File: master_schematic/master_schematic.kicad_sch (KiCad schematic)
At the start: 8 parts, among them Q1 IRLZ34NPBF, U1 teensy_4.1

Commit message: PT update
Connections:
- net GND: now also U1.USB_GND1 (USB_GND), U1.USB_GND2 (USB_GND)
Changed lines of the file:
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@@
 	(paper "A4")
+	(junction
+		(at 181.61 152.4)
+		(diameter 0)
+		(color 0 0 0 0)
+	)
 	(junction
 		(at 234.95 22.86)
@@
 	(wire
 		(pts
+			(xy 173.99 152.4) (xy 181.61 152.4)
+		)
+		(stroke
+			(width 0)
+			(type default)
+		)
+	)
+	(wire
+		(pts
 			(xy 50.8 99.06) (xy 55.88 99.06)
 		)
@@
 		)
 	)
+	(wire
+		(pts
+			(xy 184.15 50.8) (xy 184.15 55.88)
+		)
+		(stroke
+			(width 0)
+			(type default)
+		)
+	)
 	(bus
 		(pts
@@
 		)
 	)
+	(wire
+		(pts
+			(xy 181.61 149.86) (xy 181.61 152.4)
+		)
+		(stroke
+			(width 0)
+			(type default)
+		)
+	)
 	(bus
 		(pts
@@
 	(wire
 		(pts
-			(xy 181.61 55.88) (xy 173.99 55.88)
+			(xy 184.15 55.88) (xy 173.99 55.88)
 		)
 		(stroke
@@
 		)
 	)
+	(wire
+		(pts
+			(xy 201.93 55.88) (xy 201.93 62.23)
+		)
+		(stroke
+			(width 0)
+			(type default)
+		)
+	)
 	(bus
 		(pts
@@
 		(pts
 			(xy 227.33 22.86) (xy 227.33 24.13)
-		)
-		(stroke
-			(width 0)
-			(type default)
-		)
-	)
-	(wire
-		(pts
-			(xy 181.61 50.8) (xy 181.61 55.88)
 		)
 		(stroke
@@
 		)
 	)
-	(label "5V"
+	(label "+5V"
 		(at 177.8 55.88 0)
 		(fields_autoplaced yes)
@@
 		)
 	)
-	(label "5V"
+	(label "+5V"
 		(at 156.21 21.59 180)
 		(fields_autoplaced yes)
@@
 	)
 	(label "GND"
-		(at 181.61 149.86 0)
+		(at 176.53 149.86 0)
 		(fields_autoplaced yes)
 		(effects
@@
 		)
 	)
-	(label "5V"
+	(label "+5V"
 		(at 45.72 158.75 270)
 		(fields_autoplaced yes)
@@
 		)
 	)
+	(global_label "GND"
+		(shape bidirectional)
+		(at 201.93 55.88 90)
+		(fields_autoplaced yes)
+		(effects
+			(font
+				(size 1.27 1.27)
+			)
+			(justify left)
+		)
+		(property "Intersheetrefs" "${INTERSHEET_REFS}"
+			(at 201.93 47.913 90)
+			(effects
+				(font
+					(size 1.27 1.27)
+				)
+				(justify left)
+				(hide yes)
+			)
+		)
+	)
+	(global_label "+5V"
+		(shape bidirectional)
+		(at 193.04 58.42 270)
+		(fields_autoplaced yes)
+		(effects
+			(font
+				(size 1.27 1.27)
+			)
+			(justify right)
+		)
+		(property "Intersheetrefs" "${INTERSHEET_REFS}"
+			(at 193.04 66.387 90)
+			(effects
+				(font
+					(size 1.27 1.27)
+				)
+				(justify right)
+				(hide yes)
+			)
+		)
+	)
 	(symbol
 		(lib_id "power:+5V")
-		(at 181.61 50.8 0)
+		(at 184.15 50.8 0)
 		(unit 1)
 		(exclude_from_sim no)
@@
 		(fields_autoplaced yes)
 		(property "Reference" "#PWR01"
-			(at 181.61 54.61 0)
+			(at 184.15 54.61 0)
 			(effects
 				(font
@@
 		)
 		(property "Value" "+5V"
-			(at 181.61 45.72 0)
+			(at 184.15 45.72 0)
 			(effects
 				(font
@@
 		)
 		(property "Footprint" ""
-			(at 181.61 50.8 0)
+			(at 184.15 50.8 0)
 			(effects
 				(font
@@
 		)
 		(property "Datasheet" ""
-			(at 181.61 50.8 0)
+			(at 184.15 50.8 0)
 			(effects
 				(font
@@
 		)
 		(property "Description" "Power symbol creates a global label with name \"+5V\""
-			(at 181.61 50.8 0)
+			(at 184.15 50.8 0)
 			(effects
 				(font
@@
 	)
 	(symbol
+		(lib_id "power:GND")
+		(at 201.93 62.23 0)
+		(unit 1)
+		(exclude_from_sim no)
+		(in_bom yes)
+		(on_board yes)
+		(dnp no)
+		(fields_autoplaced yes)
+		(property "Reference" "#PWR016"
+			(at 201.93 68.58 0)
+			(effects
+				(font
+					(size 1.27 1.27)
+				)
+				(hide yes)
+			)
+		)
+		(property "Value" "GND"
+			(at 201.93 67.31 0)
+			(effects
+				(font
+					(size 1.27 1.27)
+				)
+			)
+		)
+		(property "Footprint" ""
+			(at 201.93 62.23 0)
+			(effects
+				(font
+					(size 1.27 1.27)
+				)
+				(hide yes)
+			)
+		)
+		(property "Datasheet" ""
+			(at 201.93 62.23 0)
+			(effects
+				(font
+					(size 1.27 1.27)
+				)
+				(hide yes)
+			)
+		)
+		(property "Description" "Power symbol creates a global label with name \"GND\" , ground"
+			(at 201.93 62.23 0)
+			(effects
+				(font
+					(size 1.27 1.27)
+				)
+				(hide yes)
+			)
+		)
+		(pin "1"
+		)
+		(instances
+			(project ""
+				(path "/c4f7e98c-e88d-49cc-9841-b70710a90a72"
+					(reference "#PWR016")
+					(unit 1)
+				)
+			)
+		)
+	)
+	(symbol
 		(lib_id "hb_symbol_lib:radio_module_900MHz")
 		(at 171.45 17.78 0)
@@
 					(unit 1)
 				)
+			)
+		)
+	)
+	(symbol
+		(lib_id "power:GND")
+		(at 181.61 152.4 0)
+		(unit 1)
+		(exclude_from_sim no)
+		(in_bom yes)
+		(on_board yes)
+		(dnp no)
+		(fields_autoplaced yes)
+		(property "Reference" "#PWR015"
+			(at 181.61 158.75 0)
+			(effects
+				(font
+					(size 1.27 1.27)
+				)
+				(hide yes)
+			)
+		)
+		(property "Value" "GND"
+			(at 181.61 157.48 0)
+			(effects
+				(font
+					(size 1.27 1.27)
+				)
+			)
+		)
+		(property "Footprint" ""
+			(at 181.61 152.4 0)
+			(effects
+				(font
+					(size 1.27 1.27)
+				)
+				(hide yes)
+			)
+		)
+		(property "Datasheet" ""
+			(at 181.61 152.4 0)
+			(effects
+				(font
+					(size 1.27 1.27)
+				)
+				(hide yes)
+			)
+		)
+		(property "Description" "Power symbol creates a global label with name \"GND\" , ground"
+			(at 181.61 152.4 0)
+			(effects
+				(font
+					(size 1.27 1.27)
+				)
+				(hide yes)
+			)
+		)
+		(pin "1"
+		)
+		(instances
+			(project ""
+				(path "/c4f7e98c-e88d-49cc-9841-b70710a90a72"
+					(reference "#PWR015")
+					(unit 1)
+				)

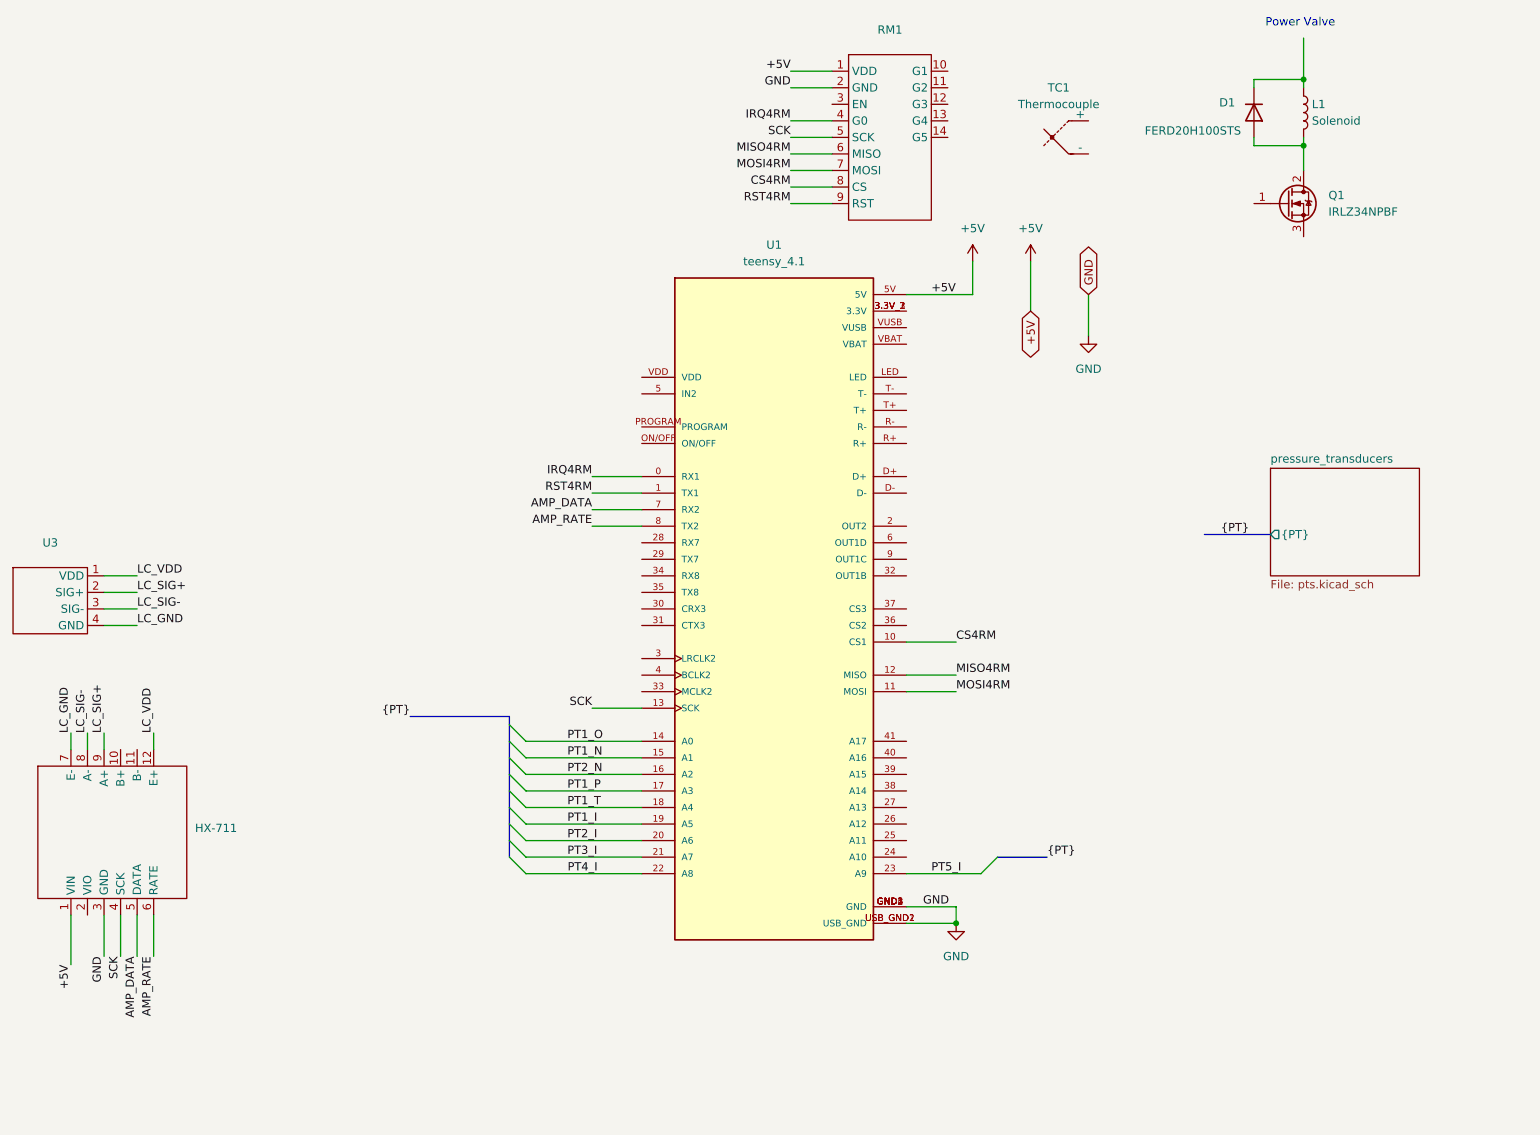
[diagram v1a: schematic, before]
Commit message: full master schematic in hierarchical format
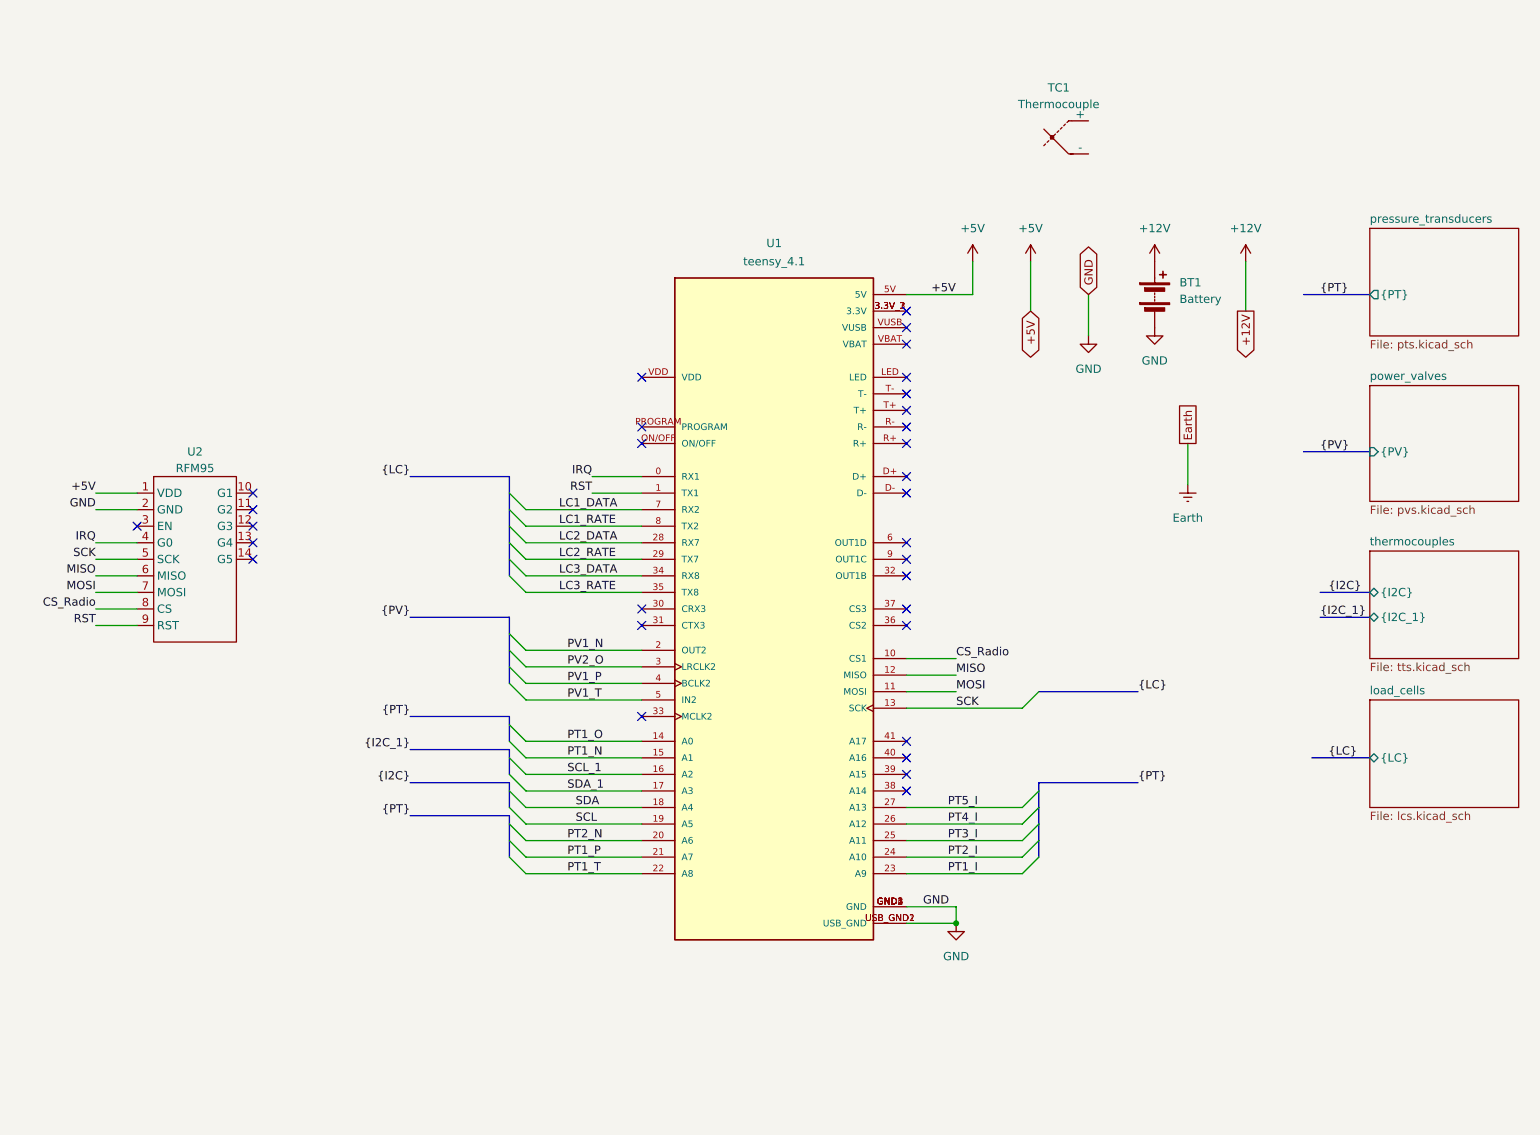
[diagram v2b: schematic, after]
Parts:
- removed D1: FERD20H100STS, symbol Device:D
- removed HX-711: ~, Connector_PinHeader_1.00mm:PinHeader_1x06_P1.00mm_Vertical, symbol hb_symbol_lib:hx711_load_cell_amplifier
- removed L1: Solenoid, symbol Device:L
- removed Q1: IRLZ34NPBF, IRLZ34NPBF:TO-220AB_INF, symbol Transistor_FET:IRLZ34N
- removed U3: ~, symbol hb_symbol_lib:new_load_cell_gx-1
- added BT1: Battery, symbol Device:Battery
- U2: renamed from RM1; value ~ -> RFM95
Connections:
- net GND: now also BT1.2 (-)
- net PT1_I: now also U1.23 (A9); no longer U1.19 (A5)
- net PT1_P: now also U1.21 (A7); no longer U1.17 (A3)
- net PT1_T: now also U1.22 (A8); no longer U1.18 (A4)
- net PT2_I: now also U1.24 (A10); no longer U1.20 (A6)
- net PT2_N: now also U1.20 (A6); no longer U1.16 (A2)
- net PT3_I: now also U1.25 (A11); no longer U1.21 (A7)
- net PT4_I: now also U1.26 (A12); no longer U1.22 (A8)
- net PT5_I: now also U1.27 (A13); no longer U1.23 (A9)
- net PV1_N: now reaches U1.2 (OUT2)
- net LC2_DATA: now reaches U1.28 (RX7)
- net LC2_RATE: now reaches U1.29 (TX7)
- net PV2_O: now reaches U1.3 (LRCLK2)
- net LC3_DATA: now reaches U1.34 (RX8)
- net LC3_RATE: now reaches U1.35 (TX8)
- net PV1_P: now reaches U1.4 (BCLK2)
- net PV1_T: now reaches U1.5 (IN2)
- net AMP_DATA renamed LC1_DATA
- net AMP_RATE renamed LC1_RATE
- net CS4RM renamed CS_Radio
- net IRQ4RM renamed IRQ
- net MISO4RM renamed MISO
- net MOSI4RM renamed MOSI
- net RST4RM renamed RST
- new net +12V: BT1.1 (+)
- new net SCL: U1.19 (A5)
- new net SCL_1: U1.16 (A2)
- new net SDA: U1.18 (A4)
- new net SDA_1: U1.17 (A3)
- no-connect marks 0 -> 31
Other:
- added sheet load_cells (lcs.kicad_sch)
- added sheet power_valves (pvs.kicad_sch)
- added sheet thermocouples (tts.kicad_sch)
- note removed: "Power Valve"
- moved on the sheet: U2

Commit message: minor updates
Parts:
- removed TC1: Thermocouple, symbol Device:Thermocouple
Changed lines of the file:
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@@
-	)
-	(symbol
-		(lib_id "Device:Thermocouple")
-		(at 199.39 31.75 0)
-		(unit 1)
-		(exclude_from_sim no)
-		(in_bom yes)
-		(on_board yes)
-		(dnp no)
-		(fields_autoplaced yes)
-		(property "Reference" "TC1"
-			(at 197.358 24.13 0)
-			(effects
-				(font
-					(size 1.27 1.27)
-				)
-			)
-		)
-		(property "Value" "Thermocouple"
-			(at 197.358 26.67 0)
-			(effects
-				(font
-					(size 1.27 1.27)
-				)
-			)
-		)
-		(property "Footprint" ""
-			(at 184.785 30.48 0)
-			(effects
-				(font
-					(size 1.27 1.27)
-				)
-				(hide yes)
-			)
-		)
-		(property "Datasheet" "~"
-			(at 184.785 30.48 0)
-			(effects
-				(font
-					(size 1.27 1.27)
-				)
-				(hide yes)
-			)
-		)
-		(property "Description" "Thermocouple"
-			(at 199.39 31.75 0)
-			(effects
-				(font
-					(size 1.27 1.27)
-				)
-				(hide yes)
-			)
-		)
-		(pin "1"
-		)
-		(pin "2"
-		)
-		(instances
-			(project "master_schematic"
-				(path "/c4f7e98c-e88d-49cc-9841-b70710a90a72"
-					(reference "TC1")
-					(unit 1)
-				)
-			)
-		)
 	)
 	(symbol

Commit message: modified for PCB development
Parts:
- added U15: EA50 Power Converter, symbol Converter_DCDC:Ag9905LP
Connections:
- net PV2_O is gone; now on net PV1_N: U1.3 (LRCLK2)
- net SCL_1 is gone; now on net PT4_I: U1.16 (A2)
- net +12V: now also U15.5 (VIN+), U15.6 (VIN+)
- net +5V: now also U15.1 (+VDC), U15.2 (+VDC)
- net GND: now also U15.3 (-VDC), U15.7 (VIN-), U15.8 (VIN-)
- net LC1_DATA: now also U1.32 (OUT1B); no longer U1.7 (RX2)
- net LC1_RATE: now also U1.31 (CTX3); no longer U1.8 (TX2)
- net LC2_DATA: now also U1.33 (MCLK2); no longer U1.28 (RX7)
- net LC2_RATE: now also U1.34 (RX8); no longer U1.29 (TX7)
- net LC3_DATA: now also U1.35 (TX8); no longer U1.34 (RX8)
- net LC3_RATE: now also U1.36 (CS2); no longer U1.35 (TX8)
- net PT1_N: now also U1.41 (A17); no longer U1.15 (A1)
- net PT1_O: now also U1.40 (A16); no longer U1.14 (A0)
- net PT1_P: now also U1.39 (A15); no longer U1.21 (A7)
- net PT1_T: now also U1.38 (A14); no longer U1.22 (A8)
- net PT2_I: now also U1.22 (A8); no longer U1.24 (A10)
- net PT3_I: now also U1.21 (A7); no longer U1.25 (A11)
- net PT4_I: no longer U1.26 (A12)
- net PT5_I: now also U1.15 (A1); no longer U1.27 (A13)
- net PV1_N: no longer U1.2 (OUT2)
- net BV1-O: now reaches U1.6 (OUT1D)
- net PT2_N: no longer names the net of U1.20 (A6)
- net SDA_1: no longer names the net of U1.17 (A3)
- new net BV1-P: U1.8 (TX2)
- new net BV1-T: U1.7 (RX2)
- new net MBV1-I-1: U1.25 (A11)
- new net MBV1-I-2: U1.26 (A12)
- new net PV1_O: U1.24 (A10)
- no-connect marks 31 -> 30
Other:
- sheet thermocouples ports: added none; removed {I2C_1}
- moved on the sheet: BT1, U1, U2
